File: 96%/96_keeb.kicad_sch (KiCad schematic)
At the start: 25 parts, among them J1 Conn_01x05, J2 USB_C_Receptacle_USB2.0, U1 STM32F072CBT6, U2 TXB0101, U3 PRTR5V0U2X, U4 XC6206PxxxMR-Regulator_Linear

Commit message: LED wiring for 96% layout
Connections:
- no-connect marks 2 -> 4
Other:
- added sheet LED Backlight (led_backlight.kicad_sch)
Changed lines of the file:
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@@
 	)
 	(no_connect
+		(at 41.91 74.93)
+	)
+	(no_connect
 		(at 45.72 160.02)
 	)
 	(no_connect
+		(at 41.91 72.39)
+	)
+	(no_connect
 		(at 45.72 162.56)
 	)
@@
 		)
 	)
+	(global_label "led_input"
+		(shape input)
+		(at 156.21 60.96 180)
+		(fields_autoplaced yes)
+		(effects
+			(font
+				(size 1.27 1.27)
+			)
+			(justify right)
+		)
+		(property "Intersheetrefs" "${INTERSHEET_REFS}"
+			(at 144.5769 60.96 0)
+			(effects
+				(font
+					(size 1.27 1.27)
+				)
+				(justify right)
+				(hide yes)
+			)
+		)
+	)
 	(global_label "col_0"
 		(shape input)
@@
 		)
 	)
+	(global_label "led_output"
+		(shape input)
+		(at 157.48 64.77 180)
+		(fields_autoplaced yes)
+		(effects
+			(font
+				(size 1.27 1.27)
+			)
+			(justify right)
+		)
+		(property "Intersheetrefs" "${INTERSHEET_REFS}"
+			(at 144.577 64.77 0)
+			(effects
+				(font
+					(size 1.27 1.27)
+				)
+				(justify right)
+				(hide yes)
+			)
+		)
+	)
 	(global_label "D+"
 		(shape input)
@@
 				)
 			)
+		)
+	)
+	(sheet
+		(at 143.51 58.42)
+		(size 15.24 8.89)
+		(exclude_from_sim no)
+		(in_bom yes)
+		(on_board yes)
+		(dnp no)
+		(fields_autoplaced yes)
+		(stroke
+			(width 0.1524)
+			(type solid)
+		)
+		(fill
+			(color 0 0 0 0.0000)
+		)
+		(property "Sheetname" "LED Backlight"
+			(at 143.51 57.7084 0)
+			(effects
+				(font
+					(size 1.27 1.27)
+				)
+				(justify left bottom)
+			)
+		)
+		(property "Sheetfile" "led_backlight.kicad_sch"
+			(at 143.51 67.8946 0)
+			(effects
+				(font
+					(size 1.27 1.27)
+				)
+				(justify left top)
+			)
+		)
+		(instances
+			(project "96_keeb"
+				(path "/cb32b2da-a60d-4ed4-a57b-2c397f553171"
+					(page "3")
+				)
+			)

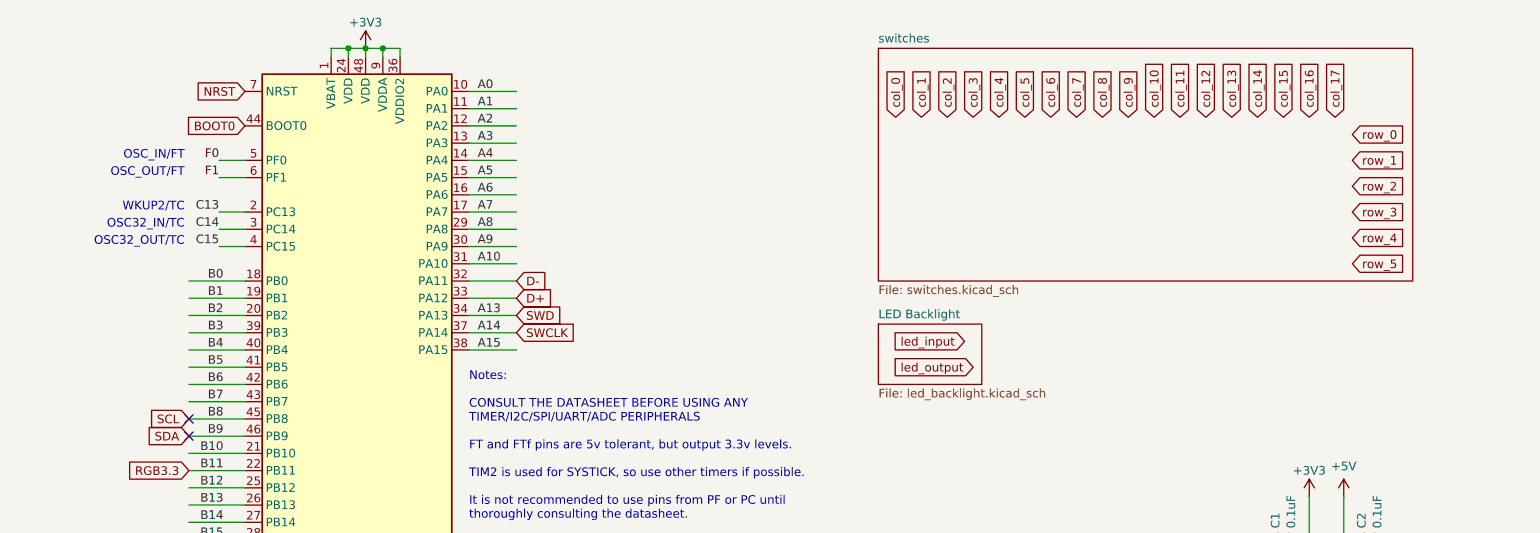
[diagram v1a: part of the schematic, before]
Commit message: Finished wiring on 96% keyboard
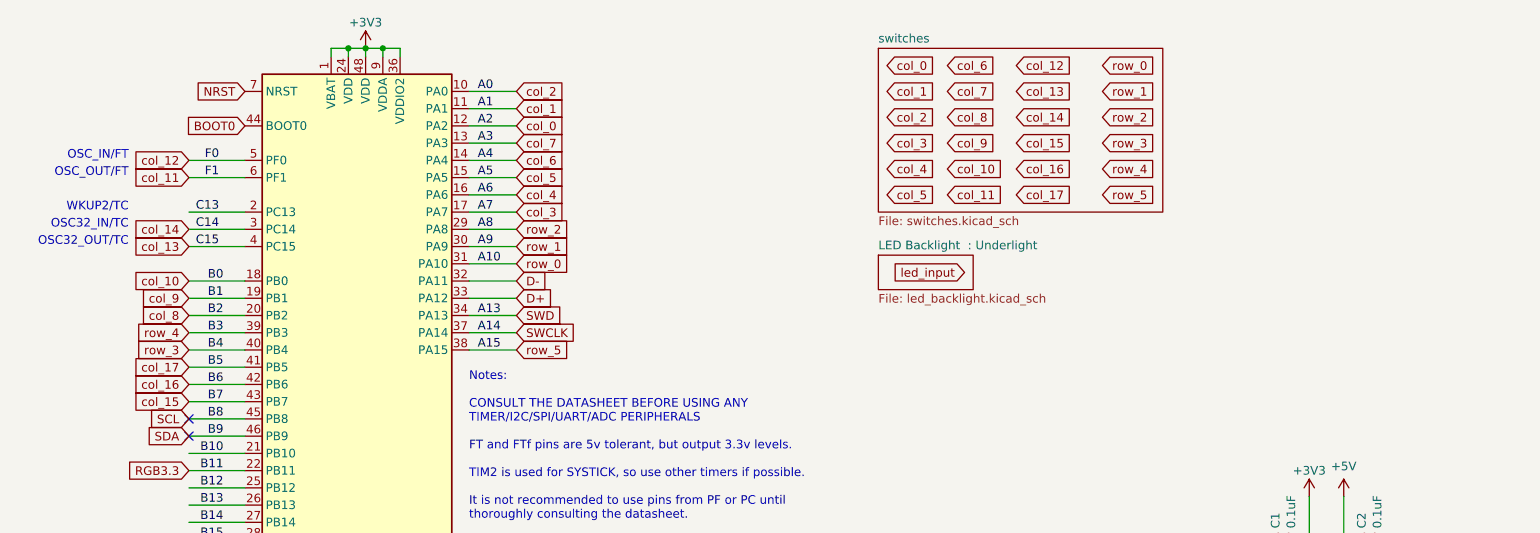
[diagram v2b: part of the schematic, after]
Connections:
- net A0 is gone; now on net col_2: U1.10 (PA0)
- net A1 is gone; now on net col_1: U1.11 (PA1)
- net A10 is gone; now on net row_0: U1.31 (PA10)
- net A15 is gone; now on net row_5: U1.38 (PA15)
- net A2 is gone; now on net col_0: U1.12 (PA2)
- net A3 is gone; now on net col_7: U1.13 (PA3)
- net A4 is gone; now on net col_6: U1.14 (PA4)
- net A5 is gone; now on net col_5: U1.15 (PA5)
- net A6 is gone; now on net col_4: U1.16 (PA6)
- net A7 is gone; now on net col_3: U1.17 (PA7)
- net A8 is gone; now on net row_2: U1.29 (PA8)
- net A9 is gone; now on net row_1: U1.30 (PA9)
- net B0 is gone; now on net col_10: U1.18 (PB0)
- net B1 is gone; now on net col_9: U1.19 (PB1)
- net B2 is gone; now on net col_8: U1.20 (PB2)
- net B3 is gone; now on net row_4: U1.39 (PB3)
- net B4 is gone; now on net row_3: U1.40 (PB4)
- net B5 is gone; now on net col_17: U1.41 (PB5)
- net B6 is gone; now on net col_16: U1.42 (PB6)
- net B7 is gone; now on net col_15: U1.43 (PB7)
- net C14 is gone; now on net col_14: U1.3 (PC14)
- net C15 is gone; now on net col_13: U1.4 (PC15)
- net F0 is gone; now on net col_12: U1.5 (PF0)
- net F1 is gone; now on net col_11: U1.6 (PF1)
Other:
- sheet LED Backlight renamed LED Backlight  : Underlight

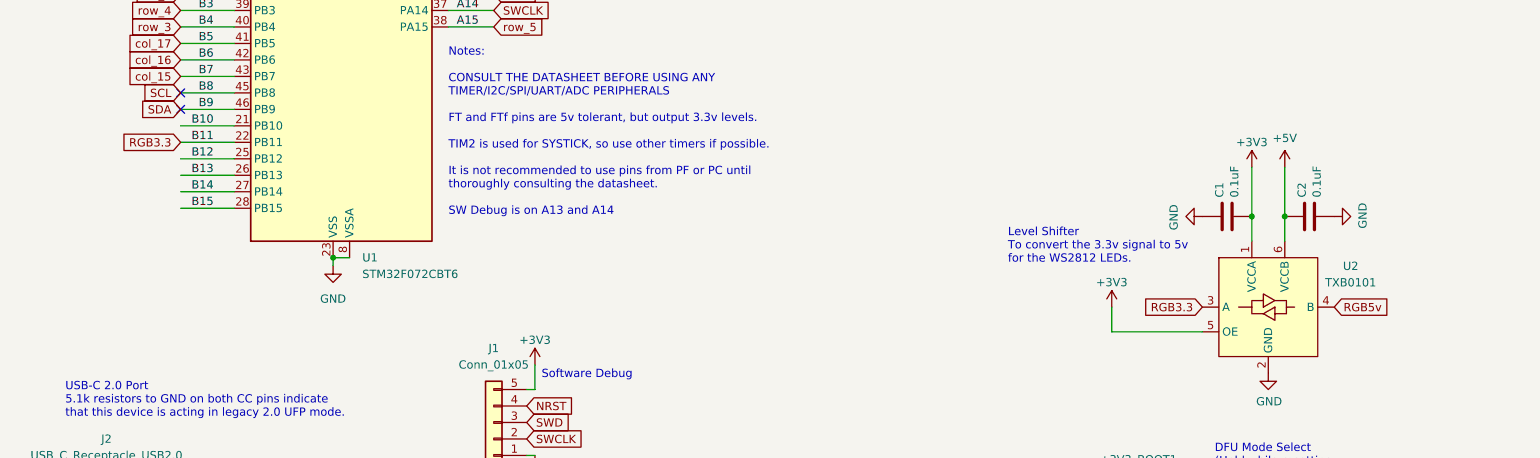
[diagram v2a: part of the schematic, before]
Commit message: Finished wiring 96% layout
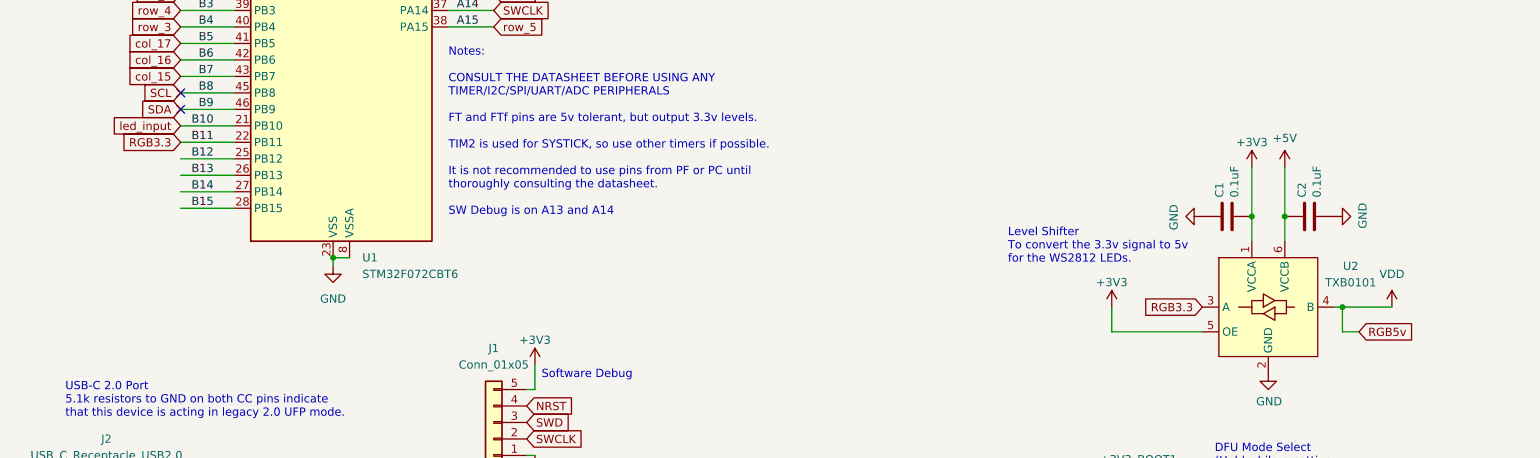
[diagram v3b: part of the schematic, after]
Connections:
- net B10 is gone; now on net led_input: U1.21 (PB10)
- net RGB5v renamed VDD
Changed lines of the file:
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@@
 	)
 	(junction
+		(at 220.98 105.41)
+		(diameter 0)
+		(color 0 0 0 0)
+	)
+	(junction
 		(at 67.945 17.78)
 		(diameter 0)
@@
 	(wire
 		(pts
+			(xy 220.98 105.41) (xy 228.6 105.41)
+		)
+		(stroke
+			(width 0)
+			(type default)
+		)
+	)
+	(wire
+		(pts
 			(xy 41.91 90.17) (xy 50.165 90.17)
 		)
@@
 	(wire
 		(pts
+			(xy 220.98 105.41) (xy 220.98 109.22)
+		)
+		(stroke
+			(width 0)
+			(type default)
+		)
+	)
+	(wire
+		(pts
 			(xy 153.67 146.05) (xy 165.1 146.05)
 		)
@@
 	(wire
 		(pts
+			(xy 220.98 109.22) (xy 223.52 109.22)
+		)
+		(stroke
+			(width 0)
+			(type default)
+		)
+	)
+	(wire
+		(pts
 			(xy 22.86 170.18) (xy 22.86 171.45)
 		)
@@
 	(wire
 		(pts
+			(xy 220.98 105.41) (xy 219.71 105.41)
+		)
+		(stroke
+			(width 0)
+			(type default)
+		)
+	)
+	(wire
+		(pts
 			(xy 89.535 153.035) (xy 89.535 156.21)
 		)
@@
 	(global_label "RGB5v"
 		(shape input)
-		(at 219.71 105.41 0)
+		(at 223.52 109.22 0)
 		(fields_autoplaced yes)
 		(effects
@@
 		)
 		(property "Intersheetrefs" "${INTERSHEET_REFS}"
-			(at 228.6823 105.41 0)
+			(at 232.4923 109.22 0)
 			(effects
 				(font
@@
 		)
 	)
+	(global_label "led_input"
+		(shape input)
+		(at 41.91 77.47 180)
+		(fields_autoplaced yes)
+		(effects
+			(font
+				(size 1.27 1.27)
+			)
+			(justify right)
+		)
+		(property "Intersheetrefs" "${INTERSHEET_REFS}"
+			(at 30.2769 77.47 0)
+			(effects
+				(font
+					(size 1.27 1.27)
+				)
+				(justify right)
+				(hide yes)
+			)
+		)
+	)
 	(global_label "col_12"
 		(shape input)
@@
 					(unit 1)
 				)
+			)
+		)
+	)
+	(symbol
+		(lib_id "power:VDD")
+		(at 228.6 105.41 0)
+		(unit 1)
+		(exclude_from_sim no)
+		(in_bom yes)
+		(on_board yes)
+		(dnp no)
+		(fields_autoplaced yes)
+		(property "Reference" "#PWR0130"
+			(at 228.6 109.22 0)
+			(effects
+				(font
+					(size 1.27 1.27)
+				)
+				(hide yes)
+			)
+		)
+		(property "Value" "VDD"
+			(at 228.6 100.33 0)
+			(effects
+				(font
+					(size 1.27 1.27)
+				)
+			)
+		)
+		(property "Footprint" ""
+			(at 228.6 105.41 0)
+			(effects
+				(font
+					(size 1.27 1.27)
+				)
+				(hide yes)
+			)
+		)
+		(property "Datasheet" ""
+			(at 228.6 105.41 0)
+			(effects
+				(font
+					(size 1.27 1.27)
+				)
+				(hide yes)
+			)
+		)
+		(property "Description" "Power symbol creates a global label with name \"VDD\""
+			(at 228.6 105.41 0)
+			(effects
+				(font
+					(size 1.27 1.27)
+				)
+				(hide yes)
+			)
+		)
+		(pin "1"
+		)
+		(instances
+			(project ""
+				(path "/cb32b2da-a60d-4ed4-a57b-2c397f553171"
+					(reference "#PWR0130")
+					(unit 1)
+				)
